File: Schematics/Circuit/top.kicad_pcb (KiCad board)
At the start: 2 copper layers, 23.5 x 23.1 mm, 13 parts, among them IC1 LPS22HB, IC3 HIH9131, J1 Conn_01x05, U1 LSM303AGRTR

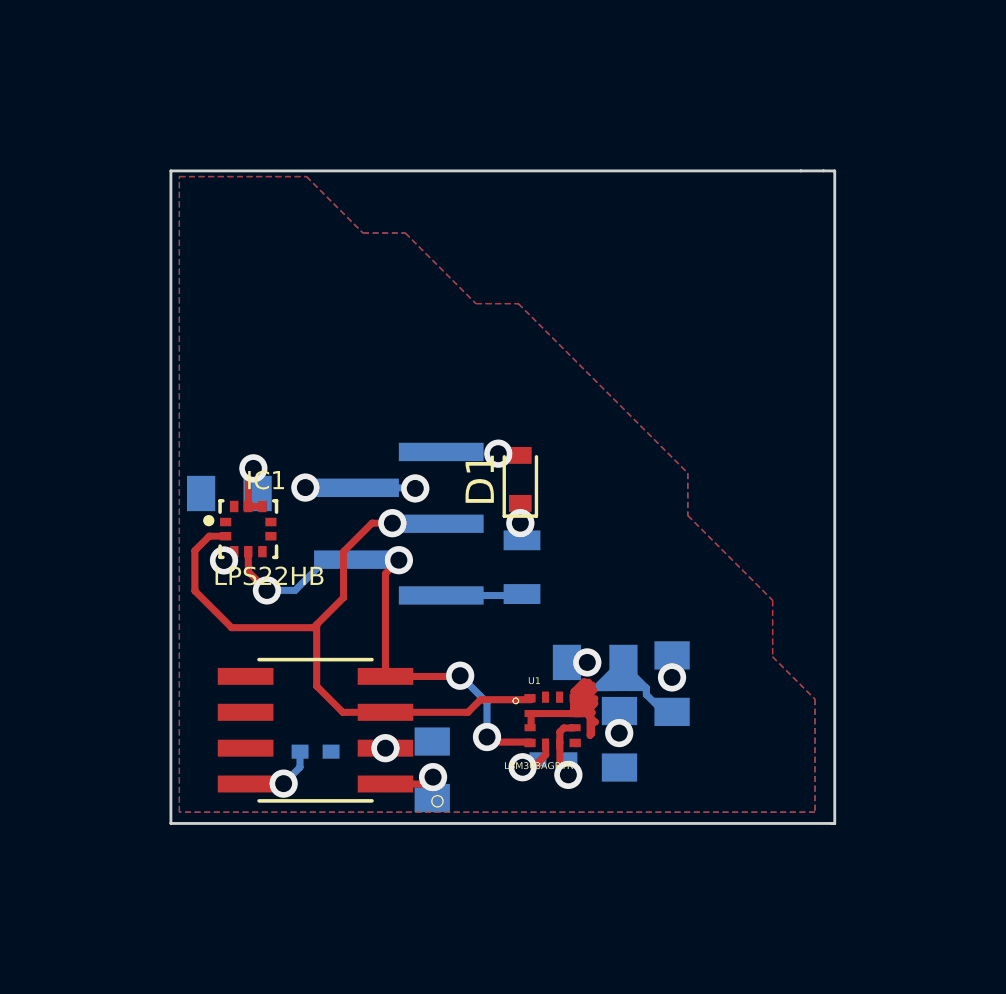
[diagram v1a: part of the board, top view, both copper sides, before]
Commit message: Edit schematic and model, add images
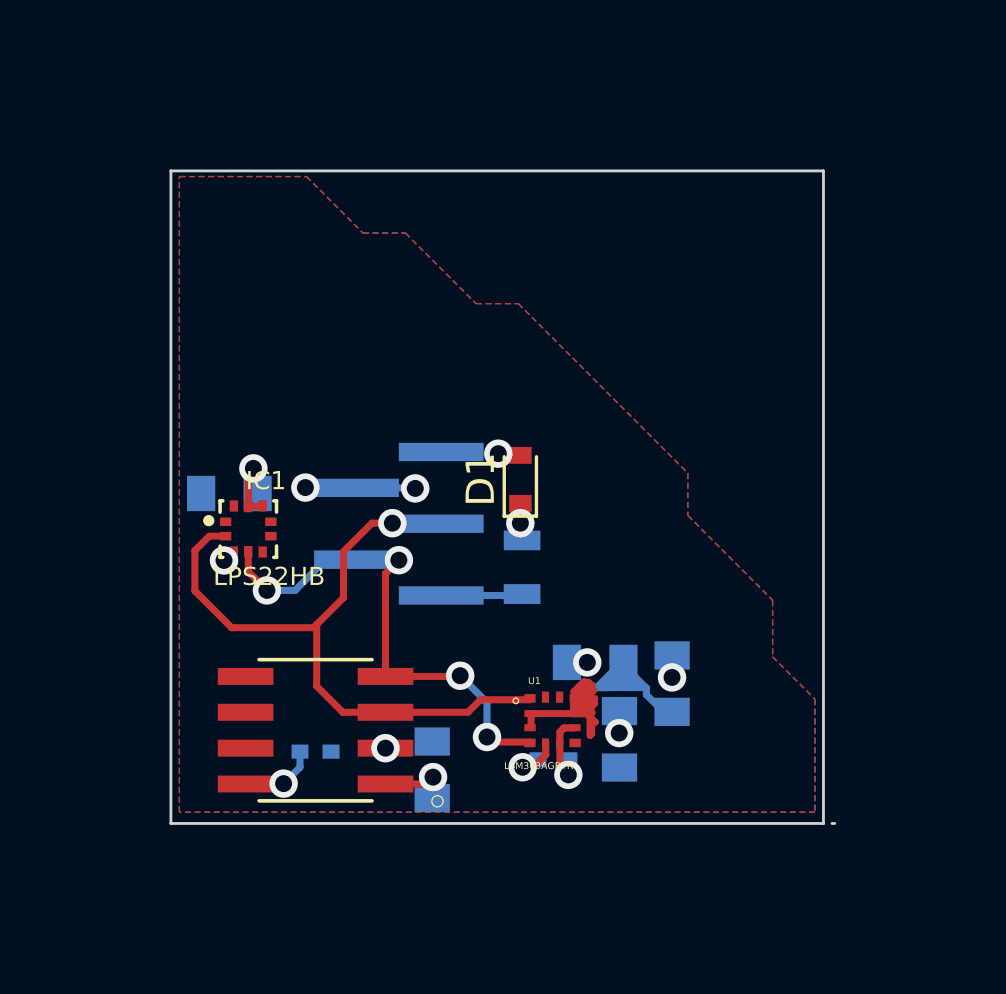
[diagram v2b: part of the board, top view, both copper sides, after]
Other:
- outline, holes or cut-outs redrawn
- net class Default: clearance 0.2 -> 0.203; via_dia 1 -> 1.006
- rule trace_clearance: 0.2 -> 0.203
- rule trace_min: 0.2 -> 0.203
- rule via_min_drill: 0.3 -> 0.6
- rule via_min_size: 0.6 -> 1.006

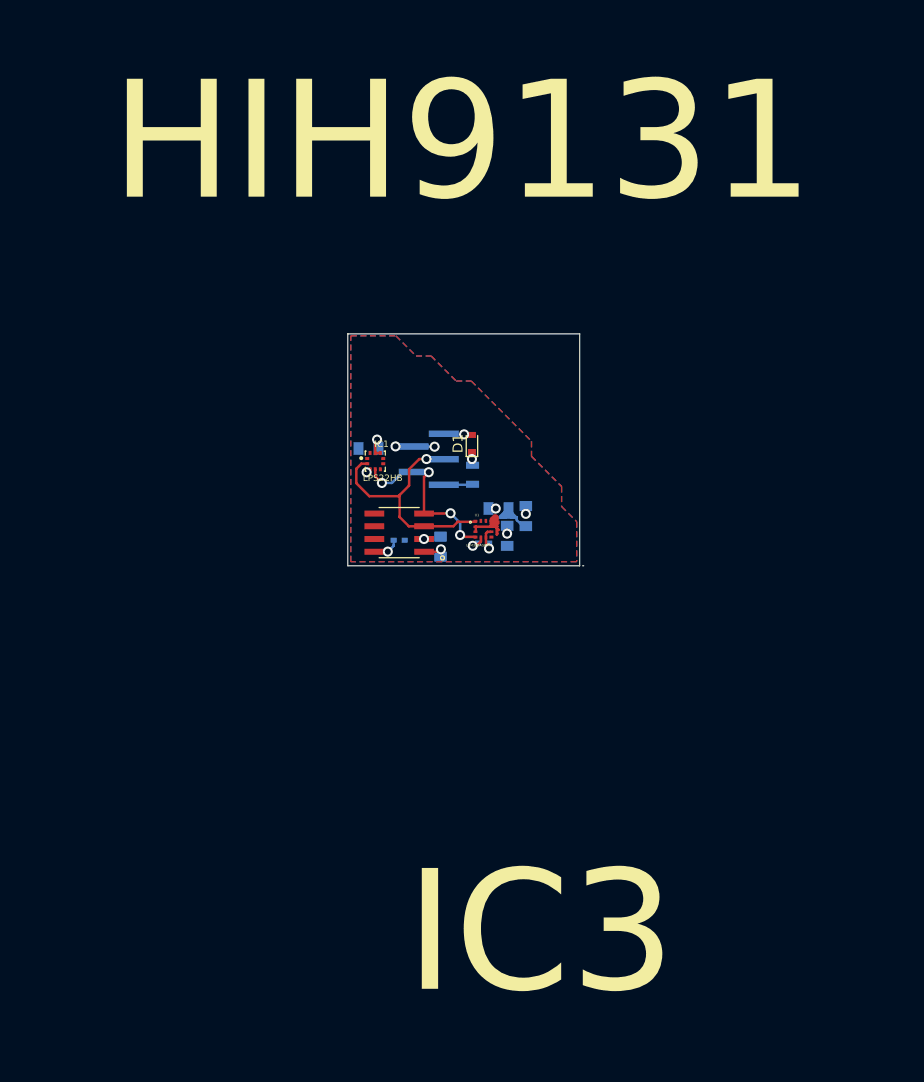
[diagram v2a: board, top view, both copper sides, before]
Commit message: Add UV and Gamma detection, fix main pcb
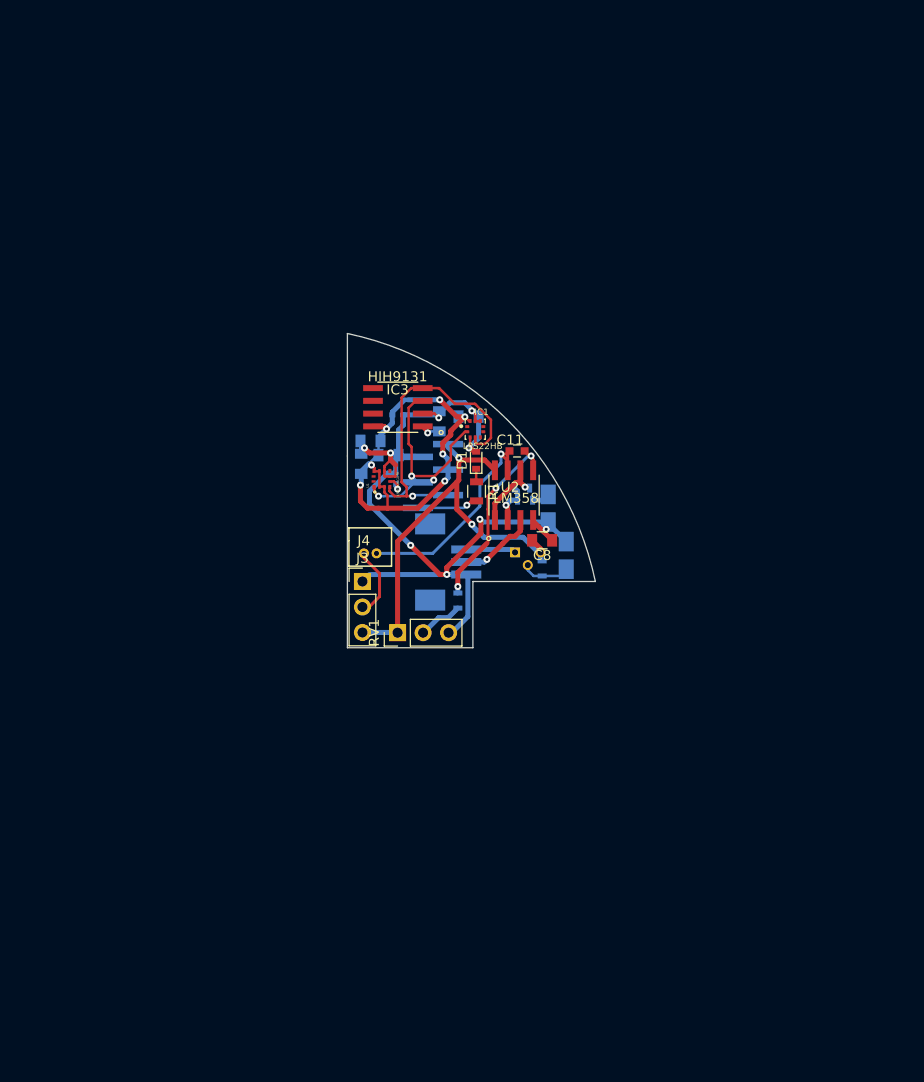
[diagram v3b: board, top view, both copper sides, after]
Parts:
- added C10: 100 uF, Capacitors_Tantalum_SMD:CP_Tantalum_Case-A_EIA-3216-18_Reflow, B.Cu at (33.6, 31.1)
- added C11: 10 nF, Capacitors_SMD:C_0603, F.Cu at (30.5, 25.4)
- added C8: 100 nF, Capacitors_SMD:C_0805, F.Cu at (33.0, 34.3)
- added C9: 100 uF, Capacitors_Tantalum_SMD:CP_Tantalum_Case-A_EIA-3216-18_Reflow, B.Cu at (35.4, 35.8)
- added J2: Conn_01x03, CanSat:MOLEX_PicoBlade_3, B.Cu at (22.9, 36.5)
- added J3: Conn_01x03, Pin_Headers:Pin_Header_Straight_1x03_Pitch2.54mm, F.Cu at (15.1, 38.4)
- added J4: Conn_01x02, CanSat:MOLEX_PicoBlade_2, F.Cu at (16.5, 35.6)
- added Q1: 2N3904, TO_SOT_Packages_THT:TO-92_Molded_Narrow, B.Cu at (30.3, 35.5)
- added R2: 150k, Resistors_SMD:R_0603, B.Cu at (33.0, 37.1)
- added R3: 1k, Resistors_SMD:R_0603, B.Cu at (31.3, 30.3)
- added R4: 1M5, Resistors_SMD:R_0603, B.Cu at (31.0, 29.1)
- added R5: 1k, Resistors_SMD:R_0603, B.Cu at (24.6, 40.3)
- added RV1: 100k, Pin_Headers:Pin_Header_Straight_1x03_Pitch2.54mm, F.Cu at (18.6, 43.5)
- added U2: LM358, SOIC127P600X175-8N:SOIC127P600X175-8N, F.Cu at (30.2, 29.8)
- J1: value Conn_01x05 -> Conn_01x06; footprint Pin_Headers:Pin_Header_Straight_1x05_Pitch1.27mm_SMD_Pin1Left -> Pin_Headers:Pin_Header_Straight_1x06_Pitch1.27mm_SMD_Pin1Left
- R1: moved to F.Cu
- moved C6 17.2 mm to (15.9, 24.4), turned to 0 degrees
- moved C7 14.4 mm to (14.9, 26.6), turned to 270 degrees
- moved C1 14.3 mm to (17.7, 25.8), turned to 180 degrees
- moved C2 12.5 mm to (18.6, 21.8)
- moved C4 12.5 mm to (22.7, 22.4)
- moved IC3 12.5 mm to (18.6, 21.0)
- moved U1 11.3 mm to (17.0, 28.2), turned to 90 degrees
- moved C3 10.9 mm to (18.4, 28.1), turned to 90 degrees
- moved IC1 10.5 mm to (26.3, 23.2)
- moved C5 10.5 mm to (25.6, 21.9)
- moved D1 1.72 mm to (26.4, 26.3)
- moved J1 1.72 mm to (22.1, 27.9)
- moved R1 1.70 mm to (26.4, 29.4)
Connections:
- IC1 pad 1: (no net) -> Net-(IC1-Pad1)
- IC1 pad 5: (no net) -> Net-(IC1-Pad5)
- IC1 pad 6: (no net) -> Net-(IC1-Pad6)
- IC1 pad 7: (no net) -> Net-(IC1-Pad7)
- IC3 pad 5: (no net) -> Net-(IC3-Pad5)
- IC3 pad 6: (no net) -> Net-(IC3-Pad6)
- IC3 pad 7: (no net) -> Net-(IC3-Pad7)
- J1 pad 1: GND -> +5V
- J1 pad 2: +3V3 -> GND
- J1 pad 3: /SCL -> +3V3
- J1 pad 4: /SDA -> /SCL
- J1 pad 5: /LED -> /SDA
- U1 pad 11: (no net) -> Net-(U1-Pad11)
- U1 pad 12: (no net) -> Net-(U1-Pad12)
- U1 pad 7: (no net) -> Net-(U1-Pad7)
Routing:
- net GND: track 18.4 -> 92.0 mm, vias 5 -> 9
- net +5V: track 0.00 -> 44.7 mm, vias 0 -> 2
- net +3V3: track 20.2 -> 45.1 mm, vias 6 -> 7
- net /GAMMA: track 0.00 -> 23.2 mm, vias 0 -> 1
- net Net-(C11-Pad2): track 0.00 -> 19.3 mm, vias 0 -> 3
- net /SDA: track 18.0 -> 31.3 mm, vias 4 -> 1
- net Net-(J2-Pad2): track 0.00 -> 7.77 mm, vias 0 -> 1
- net Net-(R4-Pad1): track 0.00 -> 7.43 mm, vias 0 -> 1
- net /UV: track 0.00 -> 7.07 mm
- net Net-(J2-Pad3): track 0.00 -> 4.98 mm
- net Net-(C9-Pad2): track 0.00 -> 4.85 mm
- net Net-(R5-Pad2): track 0.00 -> 4.47 mm
- net Net-(R3-Pad1): track 0.00 -> 4.47 mm, vias 0 -> 1
- net /LED: track 2.88 -> 6.13 mm, vias 0 -> 1
- net Net-(C10-Pad1): track 0.00 -> 1.79 mm
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- removed copper zone on F.Cu, net +3V3
- removed copper zone on B.Cu, net GND
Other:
- board size 23.5 x 23.1 mm -> 24.7 x 31.3 mm
- net class Default: via_dia 1.006 -> 0.7; via_drill 0.6 -> 0.3
- rule via_min_drill: 0.6 -> 0.3
- rule via_min_size: 1.006 -> 0.7
